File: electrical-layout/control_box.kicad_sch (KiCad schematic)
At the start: 0 parts

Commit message: layout-2025: add telemetry battery and pcb
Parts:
- added BT2: Canbat 24V ???, symbol Device:Battery_Cell
- added F6: 15A, symbol Device:Fuse
- added U14: PCB03, symbol Exocet:Telemetry_Battery_Pcb
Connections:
- new net: BT2.1 (+), F6.1
- new net: BT2.2 (-), U14. (GND)
- new net: F6.2, U14. (GND)

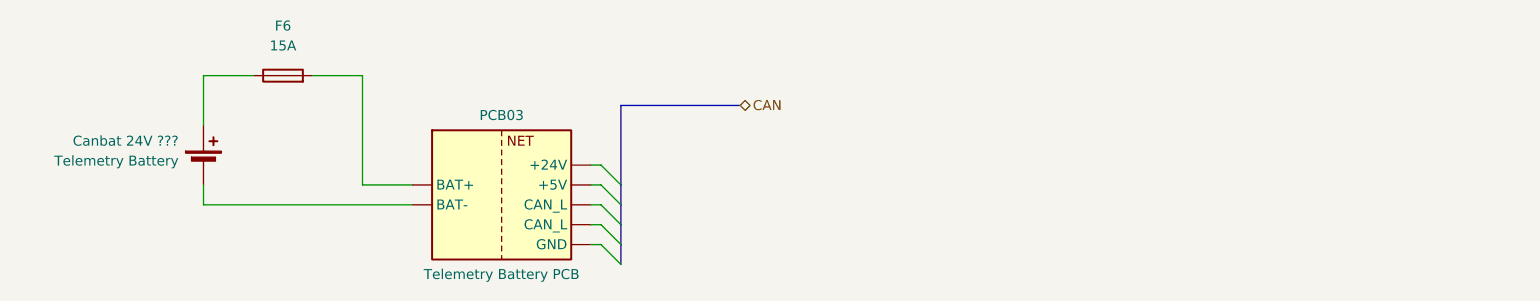
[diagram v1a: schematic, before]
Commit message: layout-2025: change to version 3.0
A few changes were made for this new version:
- Version and dates were changed on all sheets
- Added a switch (temporary symbol) after the telemetry battery
- A few notes were removed, as these have either been resolved or
discussed somewhere else
- Changed battery symbol to multi-cell battery
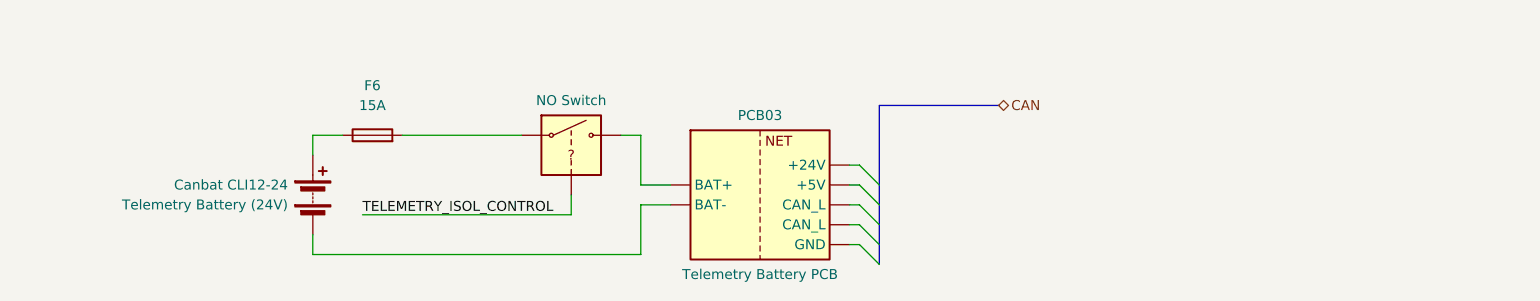
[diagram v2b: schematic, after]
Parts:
- removed BT2: Canbat 24V ???, symbol Device:Battery_Cell
- added BT3: Canbat CLI12-24, symbol Device:Battery
- added U18: NO Switch, symbol Exocet:VC_Switch_NO
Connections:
- net at F6.1: now also BT3.1 (+)
- net at U14. (GND): now also U18.
- net at F6.2: now also U18.; no longer U14. (GND)
- new net: BT3.2 (-), U14. (GND)
- new net TELEMETRY_ISOL_CONTROL: U18.
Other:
- moved on the sheet: F6

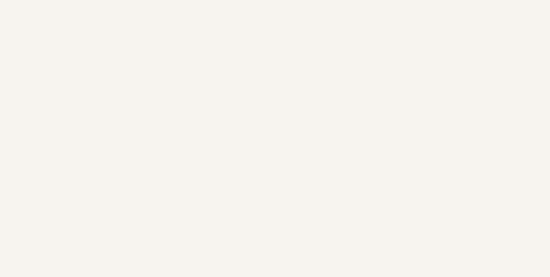
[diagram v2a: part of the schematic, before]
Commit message: layout-2025: update some power symbols
New symbol for the charge controller now has two outputs: one for the
battery and one for the load. Also, its value was replaced with "TBD"
since we haven't decided on the actual model that will be used.

Some wires were replaced with power symbols to simplify the schematic.

A symbol was created for the cooling system and it was added to the
control box page. Since little is known about this system at the
moment, it is only represented by its power inputs. This power will
come from the main energy sources (fuel cells + auxiliary battery).

Information was added about the auxiliary battery model and capacity.
Many power symbols' fields were also uniformized to separate value,
part number, description and manufacturer.
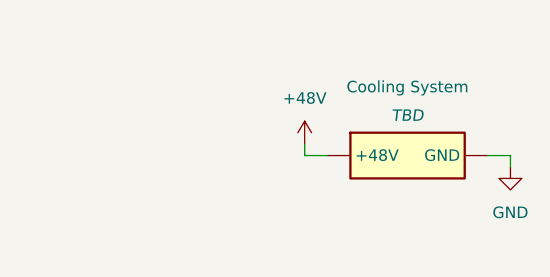
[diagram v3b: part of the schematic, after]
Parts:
- added U15: ~, symbol Exocet:Cooling_System
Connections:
- net at U14. (GND): now also U18.
- new net +48V: U15. (GND)
- new net GND: U15. (GND)
